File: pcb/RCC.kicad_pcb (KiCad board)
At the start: 2 copper layers, 25.4 x 25.4 mm, 15 parts, among them SW1 SW_MEC_5E, U1 ATtiny402-SS

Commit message: Change value of R3
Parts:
- R3: value 1Meg -> 10k
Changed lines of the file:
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@@
     (property "Sheetname" "")
     (property "Vendor" "HTL")
-    (property "VendorId" "102999")
+    (property "VendorId" "102967")
     (property "ki_description" "Resistor")
     (property "ki_keywords" "R res resistor")
@@
         (effects (font (size 0.75 0.75) (thickness 0.12)))
     )
-    (fp_text value "1Meg" (at 0 1.82 90) (layer "F.Fab")
+    (fp_text value "10k" (at 0 1.82 90) (layer "F.Fab")
         (effects (font (size 1 1) (thickness 0.15)))
     )
@@
     (pts (xy 101.6 81.28) (xy 127 81.28))
     (height -6.35)
-    (gr_text "25,40" (at 114.3 73.78) (layer "Dwgs.User")
+    (gr_text "25.40" (at 114.3 73.78) (layer "Dwgs.User")
       (effects (font (size 1 1) (thickness 0.15)))
     )
@@
     (pts (xy 106.68 76.2) (xy 106.68 101.6))
     (height 7.619999)
-    (gr_text "25,40" (at 97.910001 88.9 90) (layer "Dwgs.User")
+    (gr_text "25.40" (at 97.910001 88.9 90) (layer "Dwgs.User")
       (effects (font (size 1 1) (thickness 0.15)))
     )
@@
     (pts (xy 127 96.52) (xy 127 101.6))
     (height -2.54)
-    (gr_text "5,08" (at 128.39 99.06 90) (layer "Dwgs.User")
+    (gr_text "5.08" (at 128.39 99.06 90) (layer "Dwgs.User")
       (effects (font (size 1 1) (thickness 0.15)))
     )
@@
     (pts (xy 121.92 101.6) (xy 127 101.6))
     (height 2.54)
-    (gr_text "5,08" (at 124.46 102.99) (layer "Dwgs.User")
+    (gr_text "5.08" (at 124.46 102.99) (layer "Dwgs.User")
       (effects (font (size 1 1) (thickness 0.15)))
     )
@@
     (pts (xy 114.3 88.9) (xy 114.3 76.2))
     (height 15.24)
-    (gr_text "12,70" (at 128.39 82.55 90) (layer "User.1")
+    (gr_text "12.70" (at 128.39 82.55 90) (layer "User.1")
       (effects (font (size 1 1) (thickness 0.15)))
     )
@@
     (pts (xy 114.3 88.9) (xy 101.6 88.9))
     (height -15.24)
-    (gr_text "12,70" (at 107.95 102.99) (layer "User.1")
-      (effects (font (size 1 1) (thickness 0.15)))
-    )
+    (gr_text "12.70" (at 107.95 102.99) (layer "User.1")
+      (effects (font (size 1 1) (thickness 0.15)))
+    )

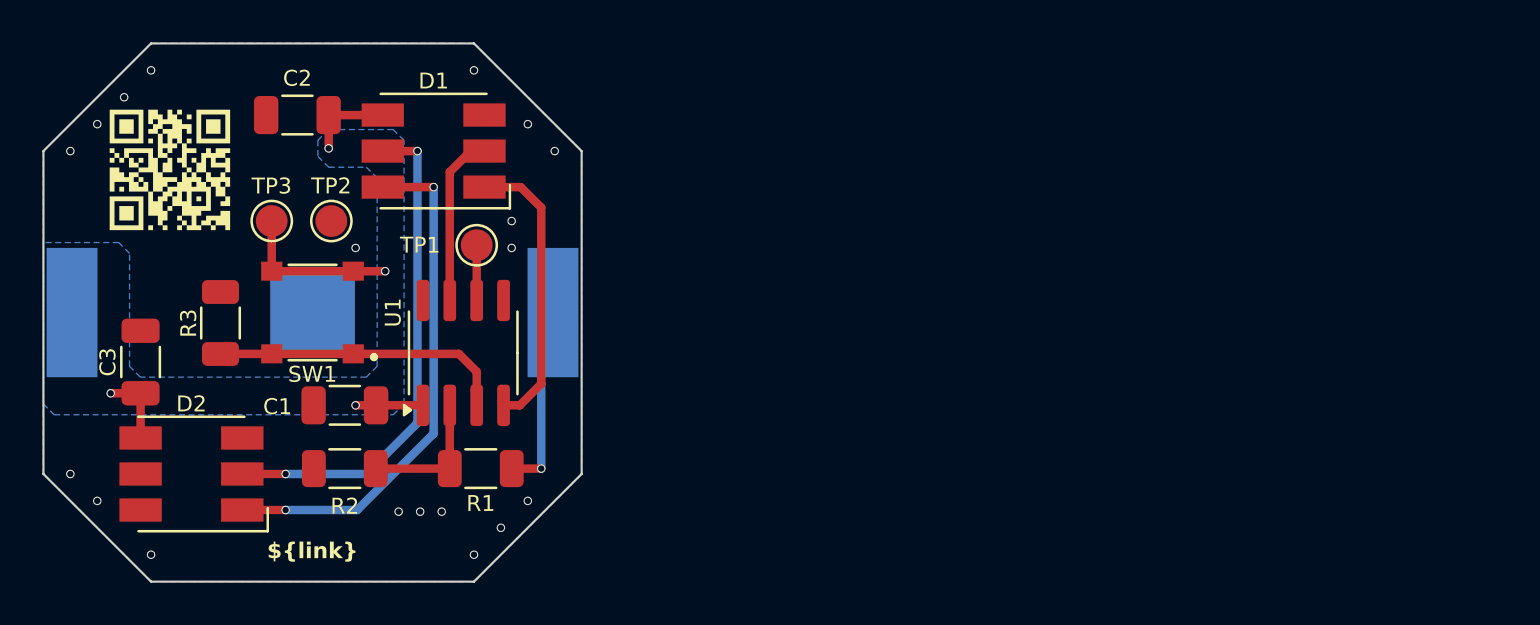
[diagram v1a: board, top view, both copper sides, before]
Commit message: Center the PCB in the middle of the drawing sheet
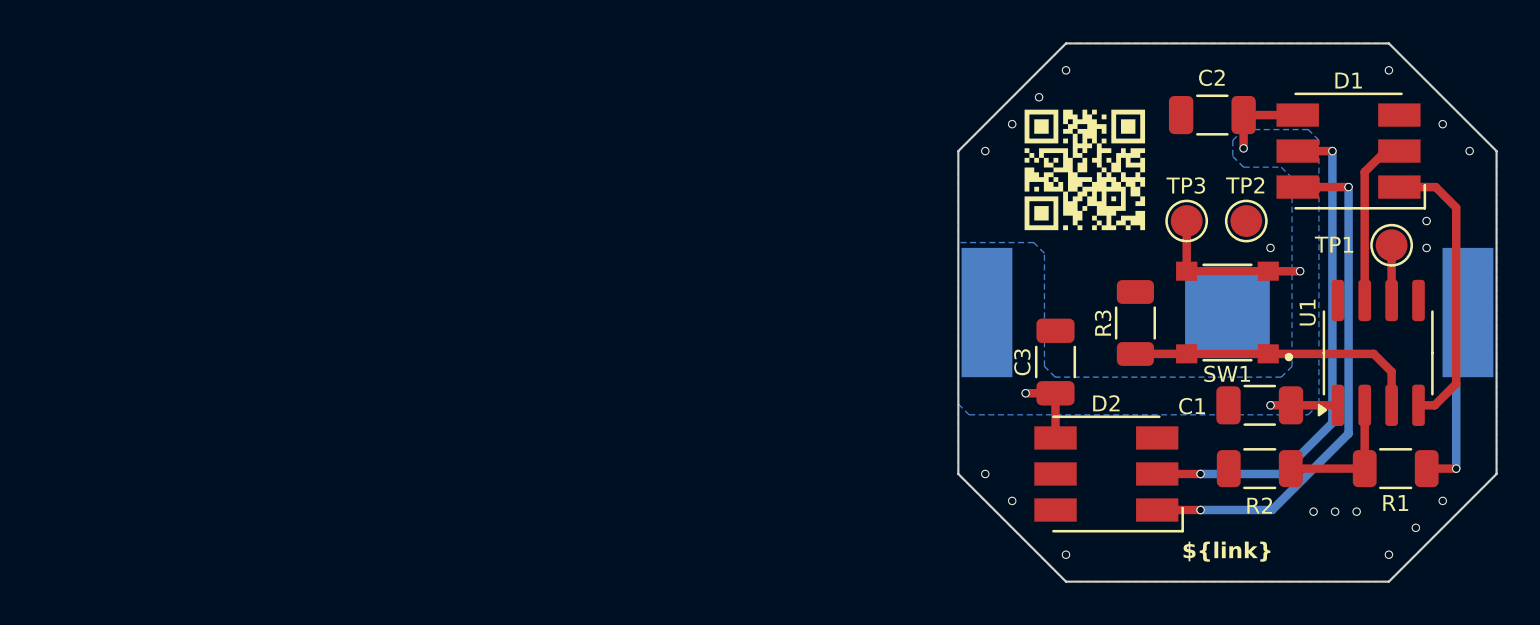
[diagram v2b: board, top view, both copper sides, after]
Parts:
- moved C3 43.2 mm to (149.4, 91.2)
- moved TP1 43.2 mm to (165.2, 85.7)
- moved TP2 43.2 mm to (158.4, 84.6)
- moved TP3 43.2 mm to (155.6, 84.6)
- moved U1 43.2 mm to (164.6, 90.8)
- moved BT1 43.2 mm to (157.5, 88.9)
- moved C1 43.2 mm to (159.0, 93.3)
- moved C2 43.2 mm to (156.8, 79.6)
- moved D1 43.2 mm to (163.2, 81.3)
- moved D2 43.2 mm to (151.8, 96.5)
- moved FID4 43.2 mm to (150.7, 82.2)
- moved R1 43.2 mm to (165.4, 96.3)
- moved R2 43.2 mm to (159.0, 96.3)
- moved R3 43.2 mm to (153.1, 89.4)
- moved SW1 43.2 mm to (157.5, 88.9)
